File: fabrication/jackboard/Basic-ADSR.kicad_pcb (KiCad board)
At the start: 2 copper layers, 20 x 109.5 mm, 13 parts, among them J1 In, J5 Conn_Jack, J6 Conn_Jack, J7 Output, Q4 BC547, SW1 Length

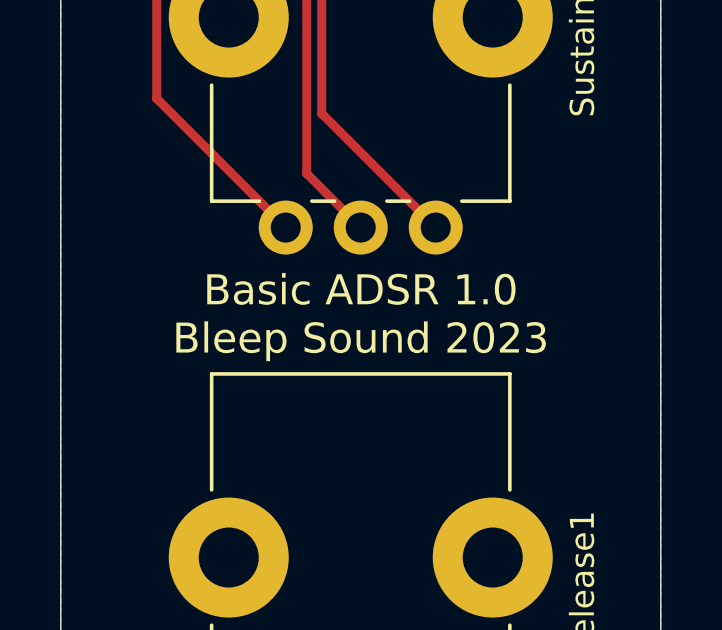
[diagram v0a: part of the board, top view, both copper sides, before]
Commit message: update GND plane for circuitboard following issues
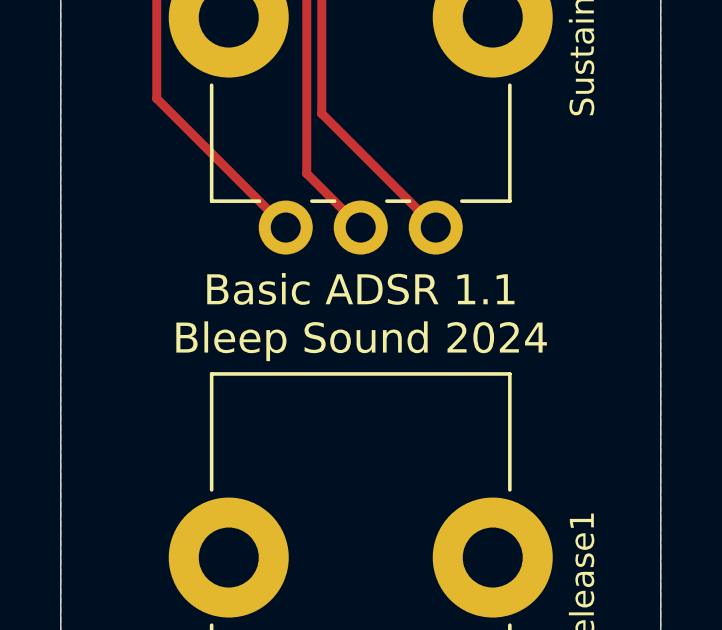
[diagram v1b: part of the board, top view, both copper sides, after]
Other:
- board text added: "Basic ADSR 1.1 Bleep Sound 2024"
- board text removed: "Basic ADSR 1.0 Bleep Sound 2023"
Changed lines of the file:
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@@
     (effects (font (size 1 1) (thickness 0.15)) (justify mirror))
   )
-  (gr_text "Basic ADSR 1.0\nBleep Sound 2023" (at 74 86.5) (layer "F.SilkS")
+  (gr_text "Basic ADSR 1.1\nBleep Sound 2024" (at 74 86.5) (layer "F.SilkS")
     (effects (font (size 1 1) (thickness 0.15)))
   )
